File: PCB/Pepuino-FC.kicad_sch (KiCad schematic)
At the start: 102 parts, among them CN1 XT30UPB-M, J1 Screw_Terminal_01x02, J2 Screw_Terminal_01x02, M1 Motor_Servo, M2 Motor_Servo, M3 Motor_Servo, M4 Motor_Servo, M5 Motor_Servo, M6 Motor_Servo, Q1 IRLML6402TRPBF-JSM, Q2 IRLML6402TRPBF-JSM, SW1 TS-1088-AR02016, SW2 TS-1088-AR02016, U1 STM32F722RETx, U2 BQ25883RGER, U3 BMP580, U4 ICM-45686, U5 TPS63070RNMR, U6 LMR51430, U7 RA-02, X1 Q13FC1350000400, X2 X322525MOB4SI

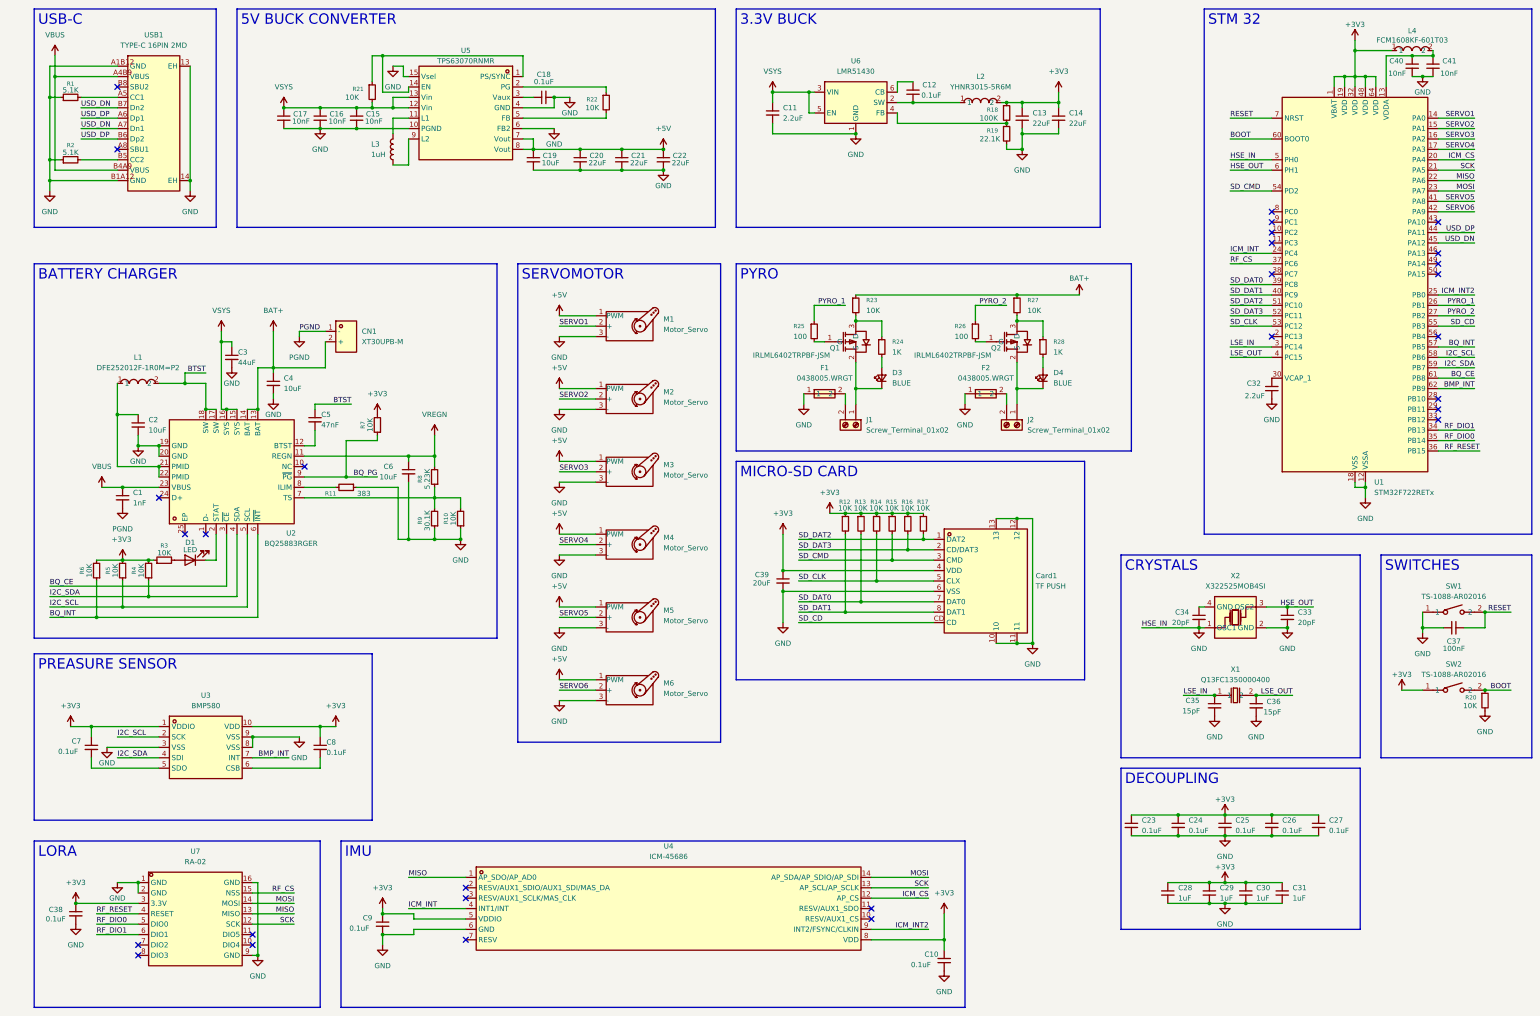
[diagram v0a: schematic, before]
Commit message: update schematic
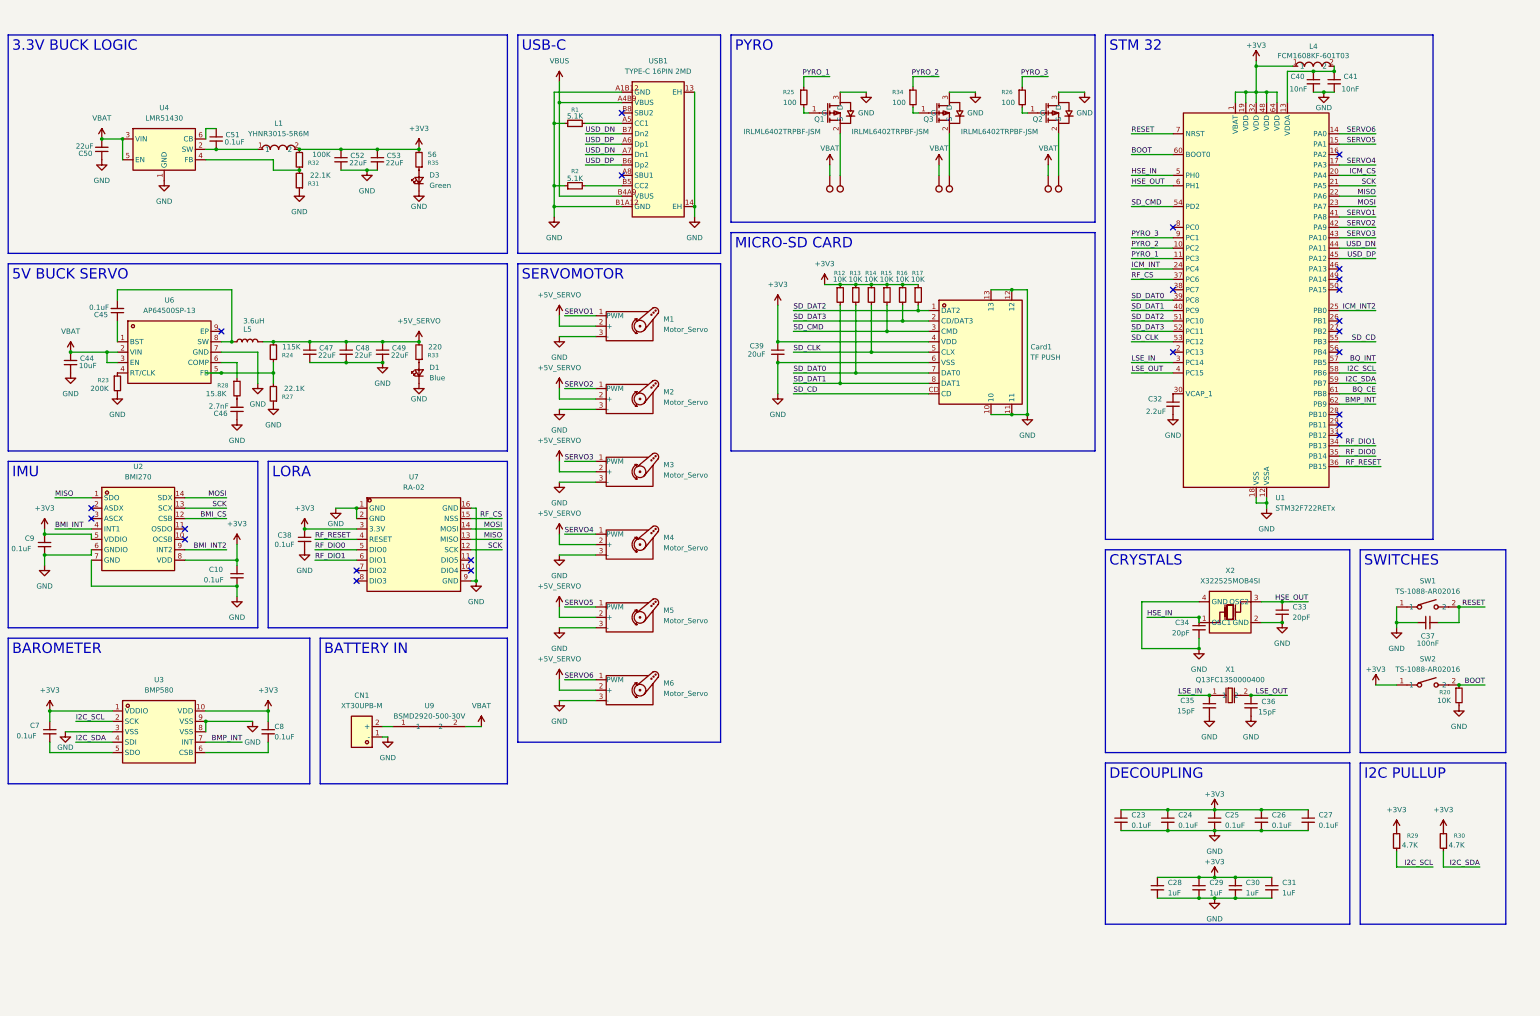
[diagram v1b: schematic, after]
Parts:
- removed C1: 1nF, Capacitor_SMD:C_0402_1005Metric, symbol Device:C_Small
- removed C11: 2.2uF, Capacitor_SMD:C_0402_1005Metric, symbol Device:C_Small
- removed C12, C18: 0.1uF, Capacitor_SMD:C_0402_1005Metric, symbol Device:C_Small
- removed C13, C14, C20, C21, C22: 22uF, Capacitor_SMD:C_0805_2012Metric, symbol Device:C_Small
- removed C15, C16, C17: 10nF, Capacitor_SMD:C_0402_1005Metric, symbol Device:C_Small
- removed C19: 10uF, Capacitor_SMD:C_0805_2012Metric, symbol Device:C_Small
- removed C2, C4, C6: 10uF, Capacitor_SMD:C_0402_1005Metric, symbol Device:C_Small
- removed C3: 44uF, Capacitor_SMD:C_0402_1005Metric, symbol Device:C_Small
- removed C5: 47nF, Capacitor_SMD:C_0402_1005Metric, symbol Device:C_Small
- removed D1: LED, LED_SMD:LED_0603_1608Metric, symbol Device:LED
- removed D4: BLUE, symbol Device:LED_Small
- removed F1, F2: 0438005.WRGT, easyEDA:F0603, symbol easyeda2kicad:0438005.WRGT
- removed J1, J2: Screw_Terminal_01x02, symbol Connector:Screw_Terminal_01x02
- removed L1: DFE252012F-1R0M=P2, easyEDA:L2520, symbol easyeda2kicad:DFE252012F-1R0M=P2
- removed L2: YHNR3015-5R6M, easyEDA:IND-SMD_L3.0-W3.0, symbol easyeda2kicad:YHNR3015-5R6M
- removed L3: 1uH, Inductor_SMD:L_0402_1005Metric, symbol Device:L
- removed R10, R21, R22, R3, R4, R5, R6, R7: 10K, Resistor_SMD:R_0201_0603Metric, symbol Device:R_Small
- removed R11: 383, Resistor_SMD:R_0201_0603Metric, symbol Device:R_Small
- removed R18: 100K, Resistor_SMD:R_0402_1005Metric, symbol Device:R_Small
- removed R19: 22.1K, Resistor_SMD:R_0201_0603Metric, symbol Device:R_Small
- removed R8: 5.23K, Resistor_SMD:R_0201_0603Metric, symbol Device:R_Small
- removed R9: 30.1K, Resistor_SMD:R_0201_0603Metric, symbol Device:R_Small
- removed U2: BQ25883RGER, easyEDA:VFQFPN-24_L4.0-W4.0-P0.50-BL-EP2.8, symbol easyeda2kicad:BQ25883RGER
- removed U4: ICM-45686, easyEDA:LGA-14_L3.0-W2.5-P0.50-TL, symbol easyeda2kicad:ICM-45686
- removed U5: TPS63070RNMR, symbol easyeda2kicad:TPS63070RNMR
- removed U6: LMR51430, Package_TO_SOT_SMD:SOT-23-6, symbol Regulator_Switching:LMR51430
- added C44: 10uF, Capacitor_SMD:C_0805_2012Metric, symbol Device:C_Small
- added C45, C51: 0.1uF, Capacitor_SMD:C_0805_2012Metric, symbol Device:C_Small
- added C46: 2.7nF, Capacitor_SMD:C_0805_2012Metric, symbol Device:C_Small
- added C47, C48, C49, C50, C52, C53: 22uF, Capacitor_SMD:C_0805_2012Metric, symbol Device:C_Small
- added D1: Blue, LED_SMD:LED_0805_2012Metric, symbol Device:LED_Small
- added L1: YHNR3015-5R6M, easyEDA:IND-SMD_L3.0-W3.0, symbol easyeda2kicad:YHNR3015-5R6M
- added L5: 3.6uH, Inductor_SMD:L_0402_1005Metric, symbol Device:L
- added Q3: IRLML6402TRPBF-JSM, easyEDA:SOT-23-3_L2.9-W1.3-P1.90-LS2.4-BR, symbol easyeda2kicad:IRLML6402TRPBF-JSM
- added R29, R30: 4.7K, Resistor_SMD:R_0201_0603Metric, symbol Device:R_Small
- added R31: 22.1K, Resistor_SMD:R_0201_0603Metric, symbol Device:R_Small
- added R32: 100K, Resistor_SMD:R_0201_0603Metric, symbol Device:R_Small
- added R33: 220, Resistor_SMD:R_0201_0603Metric, symbol Device:R_Small
- added R34: 100, Resistor_SMD:R_0201_0603Metric, symbol Device:R_Small
- added R35: 56, Resistor_SMD:R_0201_0603Metric, symbol Device:R_Small
- added TP1, TP2, TP3, TP4, TP5, TP6: TestPoint, TestPoint:TestPoint_Pad_D2.0mm, symbol Connector:TestPoint
- added U2: BMI270, easyEDA:LGA-14_L3.0-W2.5-P0.50-BR, symbol easyeda2kicad:BMI270
- added U4: LMR51430, Package_TO_SOT_SMD:SOT-23-6, symbol Regulator_Switching:LMR51430
- added U6: AP64500SP-13, easyEDA:SO-8_L4.9-W3.9-P1.27-LS6.0-BL-EP, symbol easyeda2kicad:AP64500SP-13
- added U9: BSMD2920-500-30V, easyEDA:F2920, symbol easyeda2kicad:BSMD2920-500-30V
- D3: value BLUE -> Green; footprint (none) -> LED_SMD:LED_0805_2012Metric
- M1, M2, M3, M4, M5, M6: footprint Connector_PinHeader_1.00mm:PinHeader_1x03_P1.00mm_Horizontal -> Connector_PinHeader_1.00mm:PinHeader_1x03_P1.00mm_Vertical
- R23: value 10K -> 200K
- R24: value 1K -> 115K
- R27: value 10K -> 22.1K
- R28: value 1K -> 15.8K
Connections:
- net PGND is gone; now on net GND: CN1.1 (-)
- net +3V3: now also C52.1, C53.1, L1.2, R29.2, R30.2, R32.2, R35.2, U2.5 (VDDIO), U2.8 (VDD)
- net GND: now also D3.1 (K), Q1.3 (D), Q2.3 (D), R23.2, R27.1, X2.4 (GND), C44.2, C46.1, C47.2, C48.2, C49.2, C50.1, C52.2, C53.2, D1.1 (K), Q3.3 (D), R31.1, U2.6 (GNDIO), U2.7 (GND), U4.1 (GND), U6.7 (GND); no longer U1.5 (PH0), X2.1 (OSC1)
- net I2C_SCL: now also R29.1
- net I2C_SDA: now also R30.1
- net MISO: now also U2.1 (SDO)
- net MOSI: now also U2.14 (SDX)
- net PYRO_1: now also U1.11 (PC3); no longer U1.26 (PB1)
- net PYRO_2: now also U1.10 (PC2), R34.1; no longer R26.1, U1.27 (PB2)
- net SCK: now also U2.13 (SCX)
- net SERVO1: now also M1.1 (PWM), U1.41 (PA8); no longer M1.2 (+), U1.14 (PA0)
- net SERVO2: now also M2.1 (PWM), U1.42 (PA9); no longer M2.2 (+), U1.15 (PA1)
- net SERVO3: now also M3.1 (PWM), U1.43 (PA10); no longer M3.2 (+), U1.16 (PA2)
- net SERVO4: now also M4.1 (PWM); no longer M4.2 (+)
- net SERVO5: now also M5.1 (PWM), U1.15 (PA1); no longer M5.2 (+), U1.41 (PA8)
- net SERVO6: now also M6.1 (PWM), U1.14 (PA0); no longer M6.2 (+), U1.42 (PA9)
- net USD_DN: now also U1.44 (PA11); no longer U1.45 (PA12)
- net USD_DP: now also U1.45 (PA12); no longer U1.44 (PA11)
- net at Q1.2 (S): now also TP4.1; no longer D3.1 (K)
- net at D3.2 (A): now also R35.1; no longer R24.2
- net at Q2.2 (S): now also TP1.1
- net HSE_IN: now reaches C34.1
- net HSE_IN: now also U1.5 (PH0), X2.1 (OSC1); no longer X2.4 (GND)
- net at R28.2: now also C46.2
- net PYRO_3: now reaches U1.9 (PC1)
- net PYRO_3: now also R26.1
- removed net +5V: M1.1 (PWM), M2.1 (PWM), M3.1 (PWM), M4.1 (PWM), M5.1 (PWM), M6.1 (PWM)
- removed net BAT+: CN1.2 (+), R23.1, R27.1
- new net: D1.2 (A), R33.1
- new net: CN1.2 (+), U9.1
- new net: C51.1, U4.6 (CB)
- new net: C51.2, L1.1, U4.2 (SW)
- new net: R24.1, R27.2, U6.5 (FB)
- new net: R28.1, U6.6 (COMP)
- new net: C45.1, U6.1 (BST)
- new net: R23.1, U6.4 (RT/CLK)
- new net: C45.2, L5.1, U6.8 (SW)
- new net: Q3.1 (G), R34.2
- new net: Q3.2 (S), TP6.1
- new net: R31.2, R32.1, U4.4 (FB)
- new net +5V_SERVO: C47.1, C48.1, C49.1, L5.2, M1.2 (+), M2.2 (+), M3.2 (+), M4.2 (+), M5.2 (+), M6.2 (+), R24.2, R33.2
- new net BMI_CS: U2.12 (CSB)
- new net BMI_INT: U2.4 (INT1)
- new net BMI_INT2: U2.9 (INT2)
- new net VBAT: C44.1, C50.2, TP2.1, TP3.1, TP5.1, U4.3 (VIN), U4.5 (EN), U6.2 (VIN), U6.3 (EN), U9.2
- no-connect marks 29 -> 24
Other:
- moved on the sheet: C10, C23, C24, C25, C26, C27, C28, C29, C30, C31, C32, C33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

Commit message: add final schematic
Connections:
- net ICM_CS is gone; now on net BMI_CS: U1.20 (PA4)
- net ICM_INT is gone; now on net BMI_INT: U1.24 (PC4)
- net ICM_INT2 is gone; now on net BMI_INT2: U1.25 (PB0)
- net BQ_CE: no longer names the net of U1.61 (PB8)
- net BQ_INT: no longer names the net of U1.57 (PB5)
- no-connect marks 24 -> 26
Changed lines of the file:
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@@
 	)
 	(junction
-		(at 104.14 63.5)
-		(diameter 0)
-		(color 0 0 0 0)
-	)
-	(junction
 		(at 322.58 219.71)
 		(diameter 0)
@@
 	)
 	(junction
+		(at 106.68 63.5)
+		(diameter 0)
+		(color 0 0 0 0)
+	)
+	(junction
 		(at 335.28 39.37)
 		(diameter 0)
@@
 	)
 	(no_connect
+		(at 341.63 110.49)
+	)
+	(no_connect
 		(at 129.54 161.29)
 	)
@@
 	)
 	(no_connect
+		(at 341.63 118.11)
+	)
+	(no_connect
 		(at 341.63 100.33)
 	)
@@
 	(wire
 		(pts
-			(xy 97.79 63.5) (xy 104.14 63.5)
+			(xy 97.79 63.5) (xy 106.68 63.5)
 		)
 		(stroke
@@
 	(wire
 		(pts
-			(xy 341.63 118.11) (xy 350.52 118.11)
-		)
-		(stroke
-			(width 0)
-			(type default)
-		)
-	)
-	(wire
-		(pts
 			(xy 355.6 175.26) (xy 355.6 173.99)
 		)
@@
 	(wire
 		(pts
-			(xy 341.63 110.49) (xy 350.52 110.49)
-		)
-		(stroke
-			(width 0)
-			(type default)
-		)
-	)
-	(wire
-		(pts
 			(xy 64.77 53.34) (xy 67.31 53.34)
 		)
@@
 	(wire
 		(pts
-			(xy 104.14 63.5) (xy 106.68 63.5)
-		)
-		(stroke
-			(width 0)
-			(type default)
-		)
-	)
-	(wire
-		(pts
 			(xy 323.85 146.05) (xy 323.85 144.78)
 		)
@@
 		)
 	)
-	(label "ICM_INT2"
+	(label "BMI_INT2"
 		(at 350.52 97.79 180)
 		(effects
@@
 		)
 	)
-	(label "ICM_CS"
+	(label "BMI_CS"
 		(at 350.52 64.77 180)
 		(effects
@@
 		)
 	)
-	(label "BQ_INT"
-		(at 350.52 110.49 180)
-		(effects
-			(font
-				(size 1.27 1.27)
-			)
-			(justify right bottom)
-		)
-	)
 	(label "LSE_OUT"
 		(at 328.93 191.77 180)
@@
 		)
 	)
-	(label "BQ_CE"
-		(at 350.52 118.11 180)
-		(effects
-			(font
-				(size 1.27 1.27)
-			)
-			(justify right bottom)
-		)
-	)
 	(label "RF_RESET"
 		(at 351.79 135.89 180)
@@
 		)
 	)
-	(label "ICM_INT"
+	(label "BMI_INT"
 		(at 290.83 87.63 0)
 		(effects
@@
 	(symbol
 		(lib_id "power:GND")
-		(at 104.14 63.5 0)
+		(at 106.68 63.5 0)
 		(unit 1)
 		(body_style 1)
@@
 		(fields_autoplaced yes)
 		(property "Reference" "#PWR081"
-			(at 104.14 69.85 0)
+			(at 106.68 69.85 0)
 			(hide yes)
 			(show_name no)
@@
 		)
 		(property "Value" "GND"
-			(at 104.14 68.58 0)
+			(at 106.68 68.58 0)
 			(show_name no)
 			(do_not_autoplace no)
@@
 		)
 		(property "Footprint" ""
-			(at 104.14 63.5 0)
+			(at 106.68 63.5 0)
 			(hide yes)
 			(show_name no)
@@
 		)
 		(property "Datasheet" ""
-			(at 104.14 63.5 0)
+			(at 106.68 63.5 0)
 			(hide yes)
 			(show_name no)
@@
 		)
 		(property "Description" "Power symbol creates a global label with name \"GND\" , ground"
-			(at 104.14 63.5 0)
+			(at 106.68 63.5 0)
 			(hide yes)
 			(show_name no)
